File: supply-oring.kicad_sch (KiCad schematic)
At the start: 14 parts, among them U56 LTC4358CDE, U57 LTC4358CDE, U58 LTC4358CDE

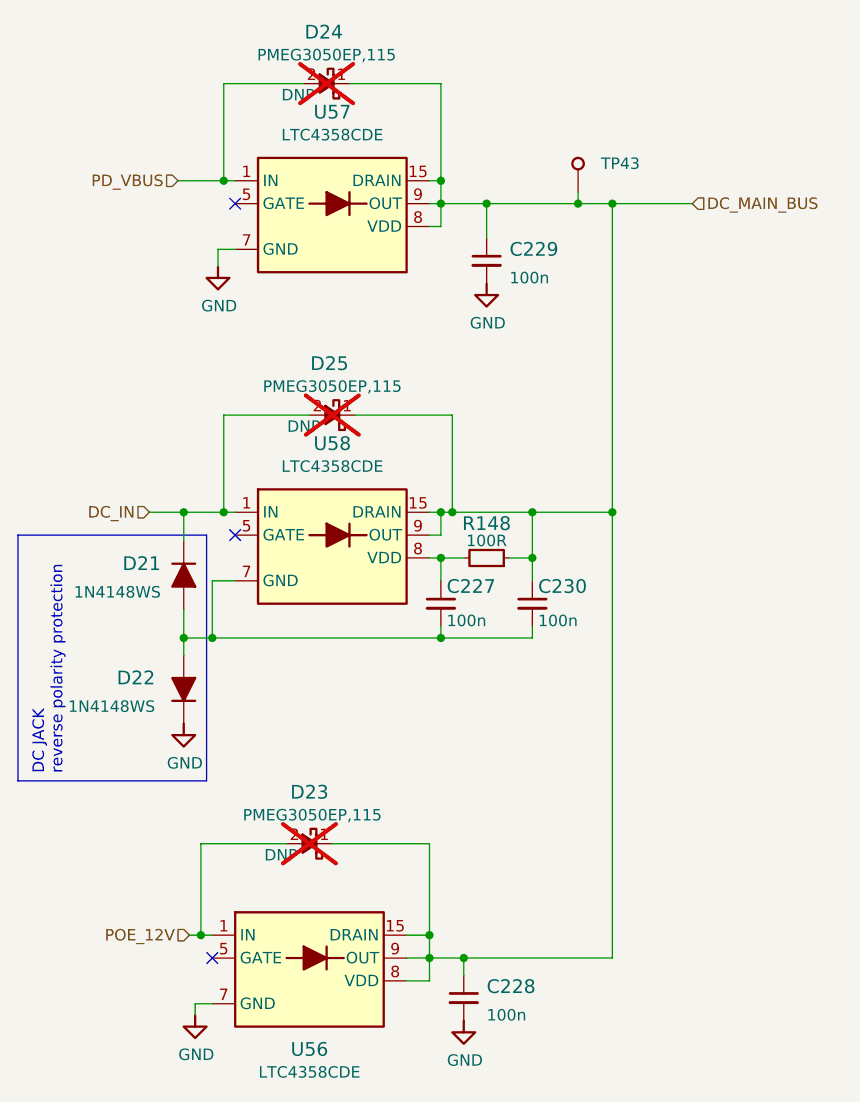
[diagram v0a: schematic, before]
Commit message: removed PoE from schematic
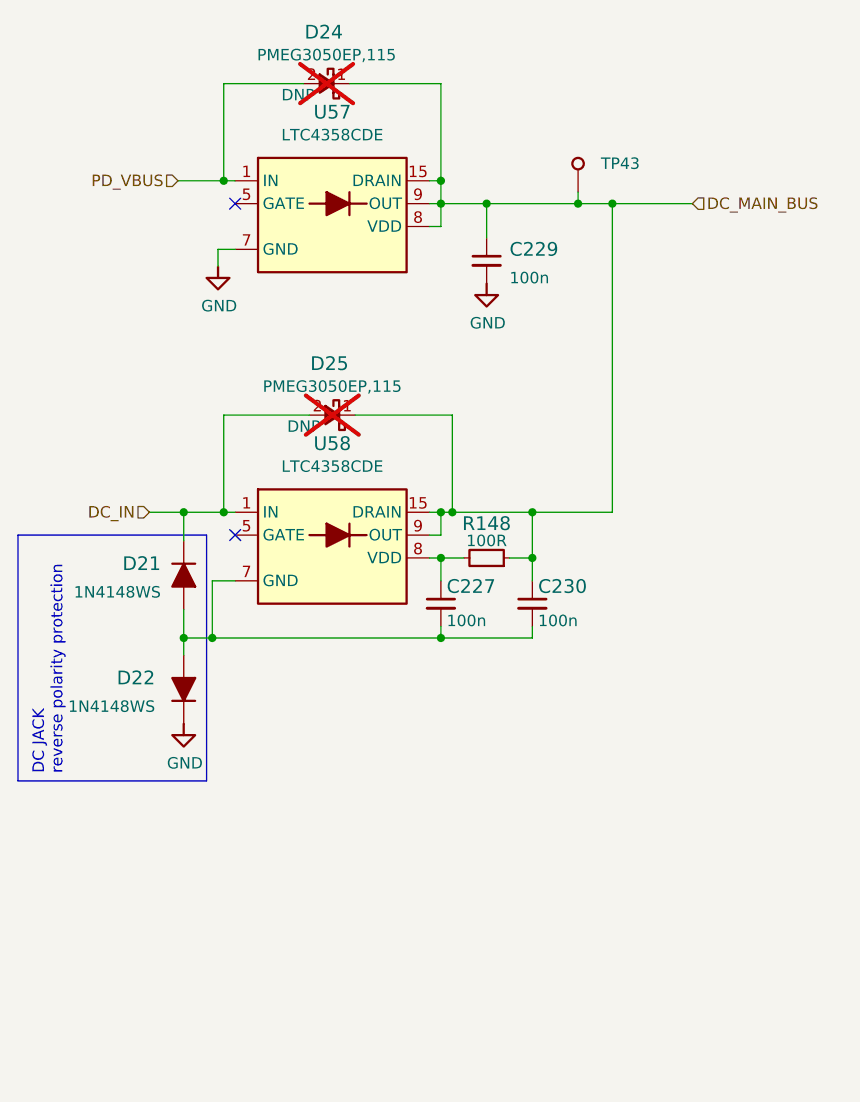
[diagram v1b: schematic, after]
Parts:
- removed C228: C_100n_0402, kria-k26-devboard-footprints:C_0402_1005Metric, symbol kria-k26-devboard:C_100n_0402
- removed D23: PMEG3050EP,115, kria-k26-devboard-footprints:Nexperia_SOD128, symbol kria-k26-devboard:PMEG3050EP,115
- removed U56: LTC4358CDE, kria-k26-devboard-footprints:DFN-14-1EP_4x3mm_P0.5mm, symbol kria-k26-devboard:LTC4358CDE
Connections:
- no-connect marks 3 -> 2
